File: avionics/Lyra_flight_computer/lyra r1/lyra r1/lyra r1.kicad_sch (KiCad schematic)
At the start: 74 parts, among them J1 USB_B_Micro, J10 BOOT 0 HEADER, J2 UART Breakout, J3 SPI Breakout, J4 I2C Breakout, J5 Screw_Terminal_01x06, J6 Conn_02x03_Top_Bottom, J7 Conn_02x03_Top_Bottom, J8 Screw_Terminal_01x06, J9 MEM2067-02-180-00-A, Q1 AO3401A, Q2 Q_NMOS_GSD, Q3 Q_NMOS_GSD, SW1 SW_MEC_5E, U1 LM317_SOT-223, U2 LM317_SOT-223, U3 USBLC6-2SC6, U4 BMI088, U5 BMP390L, U6 W25Q32JVSS, U8 STM32F103CBTx, X1 ECS-2520MV-xxx-xx

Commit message: lyra r1 work
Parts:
- removed C16: 100nf, Capacitor_SMD:C_0603_1608Metric, symbol Device:C_Small
- removed D2: LED_RBKG, LED_THT:LED_D5.0mm-4_RGB, symbol Device:LED_RBKG
- removed J3: SPI Breakout, Connector_PinHeader_2.54mm:PinHeader_1x06_P2.54mm_Vertical, symbol Connector_Generic:Conn_01x06
- removed J5, J8: Screw_Terminal_01x06, TerminalBlock:TerminalBlock_bornier-6_P5.08mm, symbol Connector:Screw_Terminal_01x06
- removed R18: 10k, Resistor_SMD:R_0603_1608Metric, symbol Device:R_Small
- removed U8: STM32F103CBTx, Package_QFP:LQFP-48_7x7mm_P0.5mm, symbol MCU_ST_STM32F1:STM32F103CBTx
- added C20, C21, C22: 100nf, Capacitor_SMD:C_0603_1608Metric, symbol Device:C_Small
- added D4: D_Small, Diode_SMD:D_0805_2012Metric, symbol Device:D_Small
- added D5: LED_ARBG, LED_SMD:LED_Cree-PLCC4_2x2mm_CW, symbol Device:LED_ARBG
- added J11, J12, J3, J5: Screw_Terminal_01x04, TerminalBlock:TerminalBlock_bornier-4_P5.08mm, symbol Connector:Screw_Terminal_01x04
- added J8: SPI Breakout, Connector_PinHeader_2.54mm:PinHeader_2x03_P2.54mm_Vertical, symbol Connector_Generic:Conn_02x03_Odd_Even
- added R16: 20k, Resistor_SMD:R_0603_1608Metric, symbol Device:R
- added R18: 6k, Resistor_SMD:R_0603_1608Metric, symbol Device:R
- added R19: 10k, Resistor_SMD:R_0603_1608Metric, symbol Device:R
- added SW2: SW_Push_DPDT, SamacSys_Parts:JS202011SCQN, symbol Switch:SW_Push_DPDT
- added U7: STM32F405RGTx, Package_QFP:LQFP-64_10x10mm_P0.5mm, symbol MCU_ST_STM32F4:STM32F405RGTx
- C13: value 100nf -> 2u2
- C14: value 10uf -> 2u2; footprint Capacitor_SMD:C_0805_2012Metric -> Capacitor_SMD:C_0603_1608Metric
- C15: value 100nf -> 1uf; footprint Capacitor_SMD:C_0603_1608Metric -> Capacitor_SMD:C_0805_2012Metric
- F1: value 1a -> 2a
- R11: value 470 -> 1k
- U3: footprint Package_TO_SOT_SMD:SOT-666 -> Package_TO_SOT_SMD:SOT-23-6
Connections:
- net +3.3VA: now also U7.13 (VDDA)
- net +3V3: now also R7.2, C20.2, C21.2, C22.2, J11.1 (Pin_1), U7.1 (VBAT), U7.19 (VDD), U7.32 (VDD), U7.48 (VDD), U7.64 (VDD); no longer C13.1, C14.2, C15.2
- net +5V: now also D4.1 (K), J11.2 (Pin_2)
- net +BATT: now also J3.4 (Pin_4), J5.1 (Pin_1), SW2.3 (C), SW2.4 (A)
- net ACCEL INT1: now also U7.34 (PB13)
- net ACCEL INT2: now also U7.33 (PB12)
- net ARM-: now also J12.1 (Pin_1), J12.3 (Pin_3), J5.2 (Pin_2), R16.1
- net BARO INT: now also U7.26 (PB0)
- net BATT SENSE: now also U7.8 (PC0)
- net BOOT0: now also R19.1, U7.60 (BOOT0); no longer J10.2 (Pin_2)
- net BUZZER: now also U7.14 (PA0)
- net CS BRKOUT: now also J8.6 (Pin_6), U7.49 (PA14)
- net CS SD: now also U7.53 (PC12)
- net FLASH CS: now also U7.50 (PA15)
- net GND: now also C14.2, C15.2, C20.1, C21.1, C22.1, J11.3 (Pin_3), J3.2 (Pin_2), J8.1 (Pin_1), R18.2, U7.12 (VSSA), U7.18 (VSS), U7.63 (VSS); no longer C14.1, C15.1, R7.1
- net GYRO INT3: now also U7.27 (PB1)
- net GYRO INT4: now also U7.28 (PB2)
- net LED BLUE: now also D5.3 (BK), U7.59 (PB7)
- net LED GREEN: now also D5.4 (GK), U7.61 (PB8)
- net LED RED: now also D5.2 (RK), U7.62 (PB9)
- net MISO: now also J8.5 (Pin_5), U7.56 (PB4)
- net MOSI: now also J8.4 (Pin_4), U7.57 (PB5)
- net OSCIN: now also U7.5 (PH0)
- net P1 EN: now also U7.51 (PC10)
- net P1-: now also J12.2 (Pin_2)
- net P2 EN: now also U7.52 (PC11)
- net P2-: now also J12.4 (Pin_4)
- net RESET: now also U7.7 (NRST)
- net SCK: now also J8.3 (Pin_3), U7.55 (PB3)
- net SCL: now also U7.29 (PB10)
- net SDA: now also U7.30 (PB11)
- net SERVO POWER: now also C15.1
- net SERVO1: now also U7.37 (PC6)
- net SERVO2: now also U7.38 (PC7)
- net SERVO3: now also U7.39 (PC8)
- net SERVO4: now also U7.40 (PC9)
- net SPI POWER: now also J8.2 (Pin_2)
- net USB D+: now also U7.45 (PA12)
- net USB D-: now also U7.44 (PA11)
- net VBUS: now also D4.2 (A)
- net +12P: now reaches F2.1, Q1.2 (S)
- net USART1 RX renamed USART2 RX
- net USART2 RX: now also U7.17 (PA3)
- net USART1 TX renamed USART2 TX
- net USART2 TX: now also U7.16 (PA2)
- new net: D5.1 (A), R7.1
- new net: J10.2 (Pin_2), R19.2
- new net: C13.1, U7.31 (VCAP_1)
- new net: C14.1, U7.47 (VCAP_2)
- new net BATT PRESWITCH: J3.1 (Pin_1), J3.3 (Pin_3), SW2.2 (B), SW2.5 (B)
- new net PA1: J11.4 (Pin_4), U7.15 (PA1)
- new net PA4: J5.4 (Pin_4), U7.20 (PA4)
- new net PB6: J5.3 (Pin_3), U7.58 (PB6)
- new net PYRO SENSE: R16.2, R18.1, U7.9 (PC1)
- no-connect marks 17 -> 32
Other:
- moved on the sheet: C1, C11, C3, D1, FB1, J1, J10, JP1, Q3, R1, R10, R12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

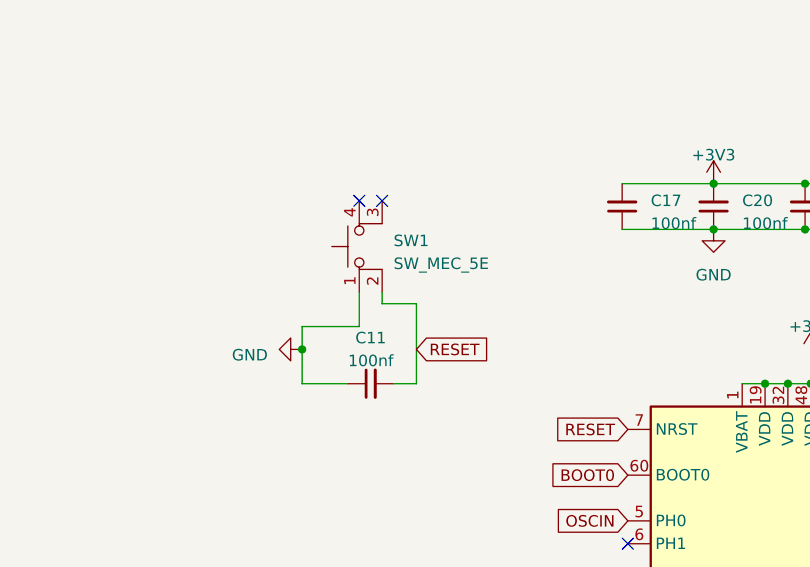
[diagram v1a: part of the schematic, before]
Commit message: lyra r1 redone with underneathdecoupling caps
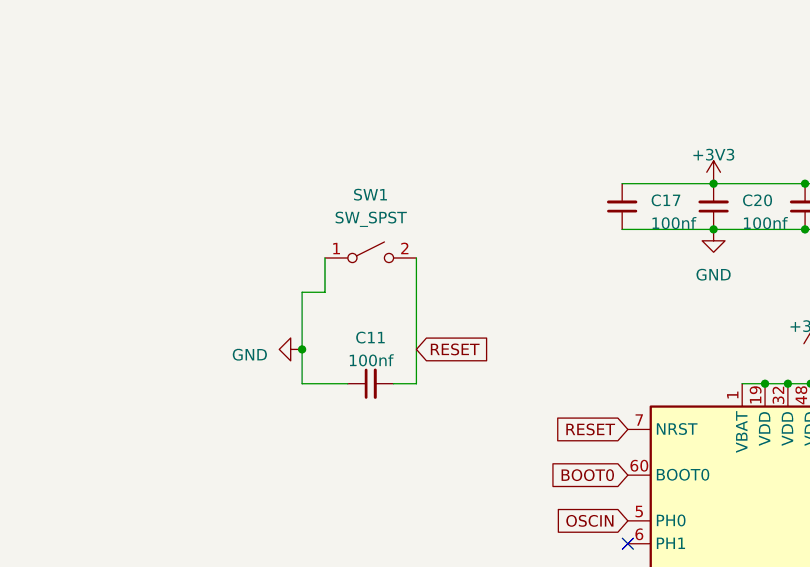
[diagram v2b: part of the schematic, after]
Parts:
- removed SW1: SW_MEC_5E, Button_Switch_THT:SW_PUSH_6mm, symbol Switch:SW_MEC_5E
- added SW1: SW_SPST, Button_Switch_SMD:SW_SPST_CK_RS282G05A3, symbol Switch:SW_SPST
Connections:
- net GND: now also SW1.1 (A)
- net RESET: now also SW1.2 (B)
- no-connect marks 32 -> 30
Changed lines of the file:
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@@
   )
   (no_connect (at 348.615 169.545))
-  (no_connect (at 283.21 121.285))
   (no_connect (at 313.055 202.565))
   (no_connect (at 313.055 205.105))
@@
   (no_connect (at 348.615 227.965))
   (no_connect (at 348.615 167.005))
-  (no_connect (at 285.75 121.285))
   (no_connect (at 313.055 164.465))
   (no_connect (at 396.24 49.53))
@@
   (no_connect (at 313.055 182.245))
   (no_connect (at 348.615 179.705))
-  (wire (pts (xy 285.75 132.715) (xy 285.75 131.445))
+  (wire (pts (xy 289.56 127.635) (xy 289.56 141.605))
     (stroke (width 0) (type default))
   )
@@
     (stroke (width 0) (type default))
   )
-  (wire (pts (xy 276.86 137.795) (xy 276.86 135.255))
+  (wire (pts (xy 276.86 137.795) (xy 276.86 131.445))
     (stroke (width 0) (type default))
   )
@@
     (stroke (width 0) (type default))
   )
-  (wire (pts (xy 276.86 135.255) (xy 283.21 135.255))
+  (wire (pts (xy 276.86 131.445) (xy 279.4 131.445))
     (stroke (width 0) (type default))
   )
@@
     (stroke (width 0) (type default))
   )
-  (wire (pts (xy 289.56 132.715) (xy 289.56 141.605))
-    (stroke (width 0) (type default))
-  )
   (wire (pts (xy 374.015 247.015) (xy 383.54 247.015))
     (stroke (width 0) (type default))
@@
     (stroke (width 0) (type default))
   )
-  (wire (pts (xy 289.56 132.715) (xy 285.75 132.715))
-    (stroke (width 0) (type default))
-  )
   (wire (pts (xy 223.52 45.72) (xy 223.52 48.26))
     (stroke (width 0) (type default))
   )
-  (wire (pts (xy 283.21 135.255) (xy 283.21 131.445))
+  (wire (pts (xy 279.4 127.635) (xy 279.4 131.445))
     (stroke (width 0) (type default))
   )
@@
     )
   )
+  (symbol (lib_id "Switch:SW_SPST") (at 284.48 127.635 0) (unit 1)
+    (in_bom yes) (on_board yes) (dnp no) (fields_autoplaced)
+    (property "Reference" "SW1" (at 284.48 120.65 0)
+      (effects (font (size 1.27 1.27)))
+    )
+    (property "Value" "SW_SPST" (at 284.48 123.19 0)
+      (effects (font (size 1.27 1.27)))
+    )
+    (property "Footprint" "Button_Switch_SMD:SW_SPST_CK_RS282G05A3" (at 284.48 127.635 0)
+      (effects (font (size 1.27 1.27)) hide)
+    )
+    (property "Datasheet" "~" (at 284.48 127.635 0)
+      (effects (font (size 1.27 1.27)) hide)
+    )
+    (pin "1")
+    (pin "2")
+    (instances
+      (project "lyra r1"
+        (path "/0420b479-31be-4cce-8403-e78e0e884a5a"
+          (reference "SW1") (unit 1)
+        )
+      )
+    )
+  )
   (symbol (lib_id "power:GND") (at 165.1 237.49 270) (unit 1)
     (in_bom yes) (on_board yes) (dnp no) (fields_autoplaced)
@@
         )
       )
-    )
-  )
-  (symbol (lib_id "Switch:SW_MEC_5E") (at 285.75 126.365 90) (unit 1)
-    (in_bom yes) (on_board yes) (dnp no) (fields_autoplaced)
-    (property "Reference" "SW1" (at 287.02 125.73 90)
-      (effects (font (size 1.27 1.27)) (justify right))
-    )
-    (property "Value" "SW_MEC_5E" (at 287.02 128.27 90)
-      (effects (font (size 1.27 1.27)) (justify right))
-    )
-    (property "Footprint" "Button_Switch_THT:SW_PUSH_6mm" (at 278.13 126.365 0)
-      (effects (font (size 1.27 1.27)) hide)
-    )
-    (property "Datasheet" "http://www.apem.com/int/index.php?controller=attachment&id_attachment=1371" (at 278.13 126.365 0)
-      (effects (font (size 1.27 1.27)) hide)
-    )
-    (pin "1")
-    (pin "2")
-    (pin "3")
-    (pin "4")
-    (instances
-      (project "lyra r1"
-        (path "/0420b479-31be-4cce-8403-e78e0e884a5a"
-          (reference "SW1") (unit 1)
-        )
-      )
-      (project "wolf flight comp"
-        (path "/9d66d0de-4b18-4272-a275-a6876d38a7f9"
-          (reference "SW1") (unit 1)
-        )
-      )

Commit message: lyra work and exporting to jlcpcb
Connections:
- net +12P: now also J5.1 (Pin_1)
- net +BATT: no longer J5.1 (Pin_1)
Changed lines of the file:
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@@
+    )
+  )
+  (symbol (lib_id "power:+12P") (at 243.84 270.51 90) (unit 1)
+    (in_bom yes) (on_board yes) (dnp no) (fields_autoplaced)
+    (property "Reference" "#PWR044" (at 247.65 270.51 0)
+      (effects (font (size 1.27 1.27)) hide)
+    )
+    (property "Value" "+12P" (at 240.03 270.51 90)
+      (effects (font (size 1.27 1.27)) (justify left))
+    )
+    (property "Footprint" "" (at 243.84 270.51 0)
+      (effects (font (size 1.27 1.27)) hide)
+    )
+    (property "Datasheet" "" (at 243.84 270.51 0)
+      (effects (font (size 1.27 1.27)) hide)
+    )
+    (pin "1")
+    (instances
+      (project "lyra r1"
+        (path "/0420b479-31be-4cce-8403-e78e0e884a5a"
+          (reference "#PWR044") (unit 1)
+        )
+      )
     )
   )
@@
         )
       )
-    )
-  )
-  (symbol (lib_id "power:+BATT") (at 243.84 270.51 90) (unit 1)
-    (in_bom yes) (on_board yes) (dnp no)
-    (property "Reference" "#PWR044" (at 247.65 270.51 0)
-      (effects (font (size 1.27 1.27)) hide)
-    )
-    (property "Value" "+BATT" (at 240.665 270.51 90)
-      (effects (font (size 1.27 1.27)) (justify left))
-    )
-    (property "Footprint" "" (at 243.84 270.51 0)
-      (effects (font (size 1.27 1.27)) hide)
-    )
-    (property "Datasheet" "" (at 243.84 270.51 0)
-      (effects (font (size 1.27 1.27)) hide)
-    )
-    (pin "1")
-    (instances
-      (project "lyra r1"
-        (path "/0420b479-31be-4cce-8403-e78e0e884a5a"
-          (reference "#PWR044") (unit 1)
-        )
-      )
-      (project "wolf flight comp"
-        (path "/9d66d0de-4b18-4272-a275-a6876d38a7f9"
-          (reference "#PWR040") (unit 1)
-        )
-      )
